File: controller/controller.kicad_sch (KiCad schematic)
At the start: 0 parts

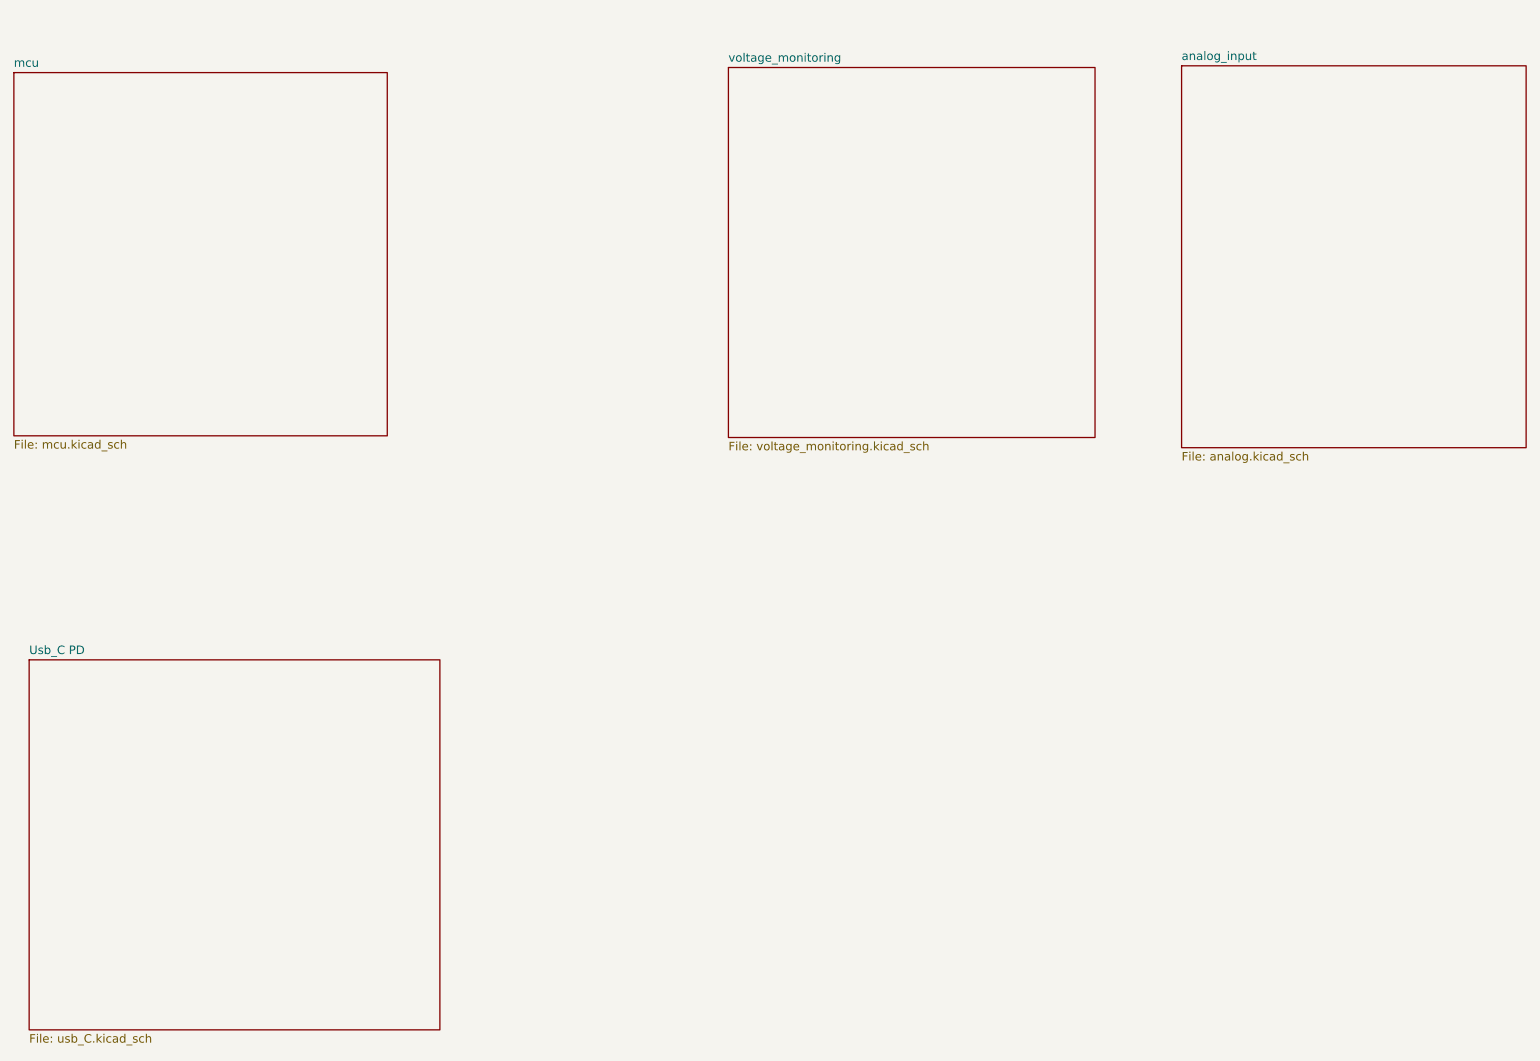
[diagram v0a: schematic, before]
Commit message: Controller Complete
Completed Controller Section
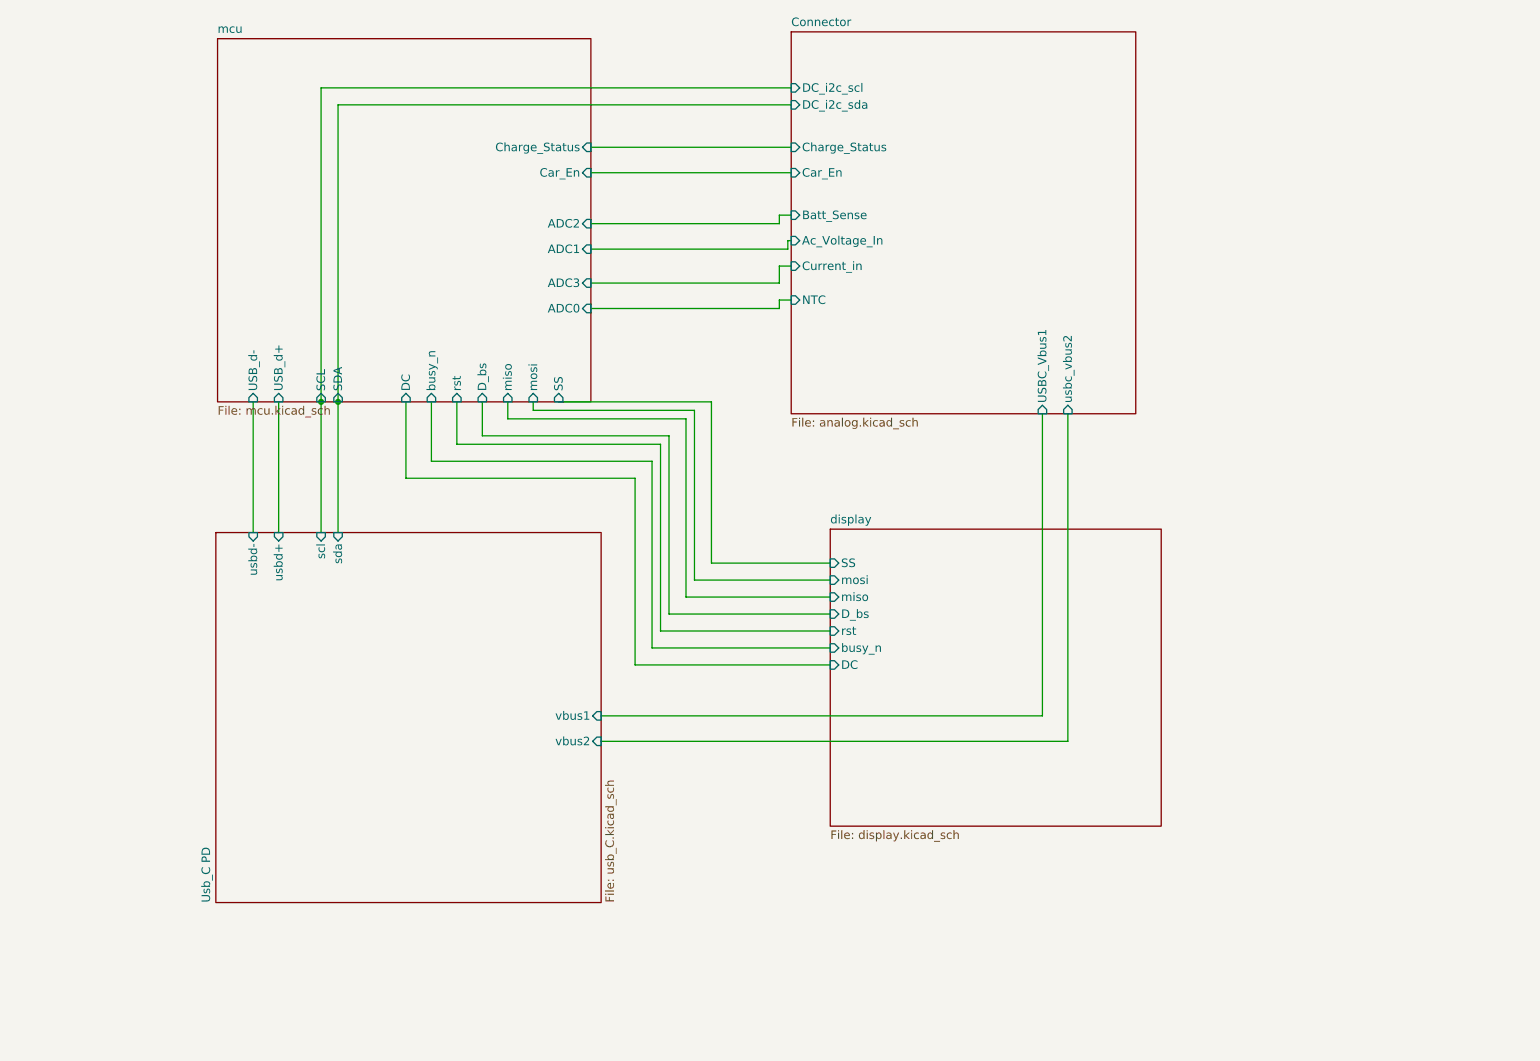
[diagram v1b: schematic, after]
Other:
- sheet analog_input renamed Connector
- removed sheet voltage_monitoring
- added sheet display (display.kicad_sch)
- sheet Connector ports: added Ac_Voltage_In, Batt_Sense, Car_En, Charge_Status, Current_in, DC_i2c_scl, DC_i2c_sda, NTC, USBC_Vbus1, usbc_vbus2; removed none
- sheet Usb_C PD ports: added scl, sda, usbd+, usbd-, vbus1, vbus2; removed none
- sheet mcu ports: added ADC0, ADC1, ADC2, ADC3, Car_En, Charge_Status, DC, D_bs, SCL, SDA, SS, USB_d+, USB_d-, busy_n, miso, mosi, rst; removed none
- company: (none) -> Voltaworks
